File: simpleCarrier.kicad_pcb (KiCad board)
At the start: 4 copper layers, 103 x 99 mm, 132 parts, among them CN1 KH-CL0.5-H2.0-22PIN, CN2 KH-CL0.5-H2.0-22PIN, IC2 RT9187CGB, J1 USB_B, J10 Conn_01x03_Socket, J11 Conn_01x05_Socket, J2 RJ45_RB1-125B8G1A, J3 USB_B, J4 SFW15R-1STE1LF, J5 SFW15R-1STE1LF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

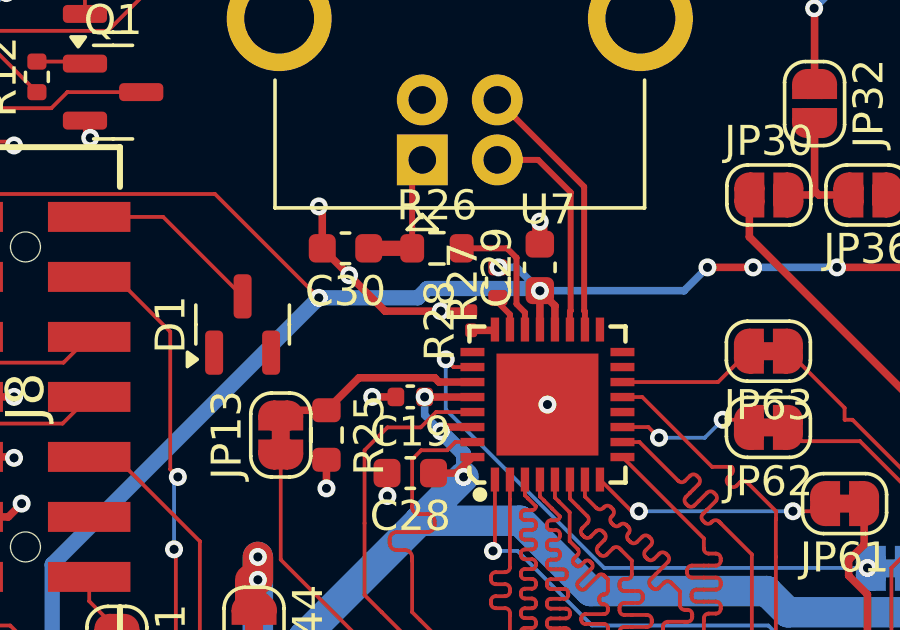
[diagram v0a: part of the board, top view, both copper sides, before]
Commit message: removed all resistors 0201mm, changed to 0402mm
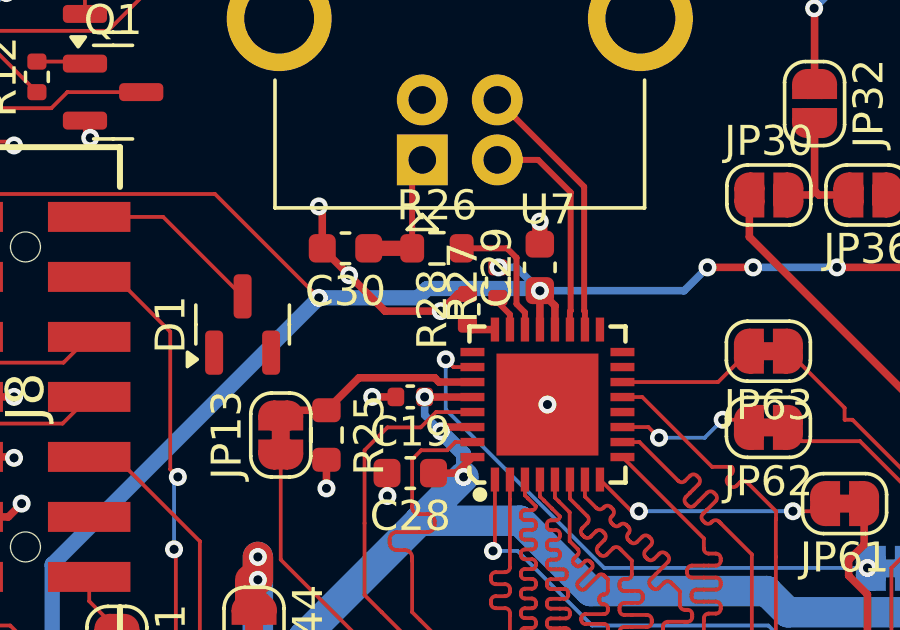
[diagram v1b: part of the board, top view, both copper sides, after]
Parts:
- R28: footprint Resistor_SMD:R_0201_0603Metric -> Resistor_SMD:R_0402_1005Metric
- moved R28 0.40 mm to (116.0, 63.9)

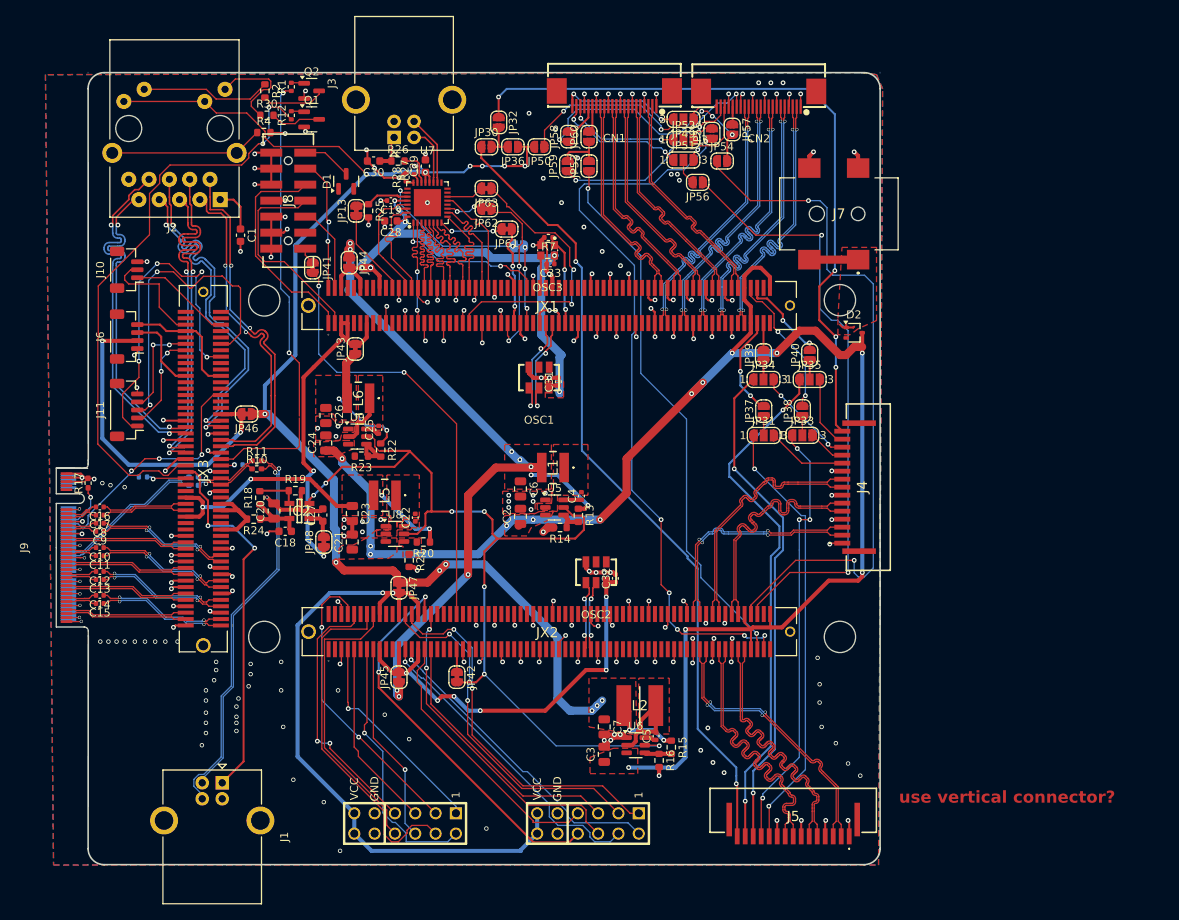
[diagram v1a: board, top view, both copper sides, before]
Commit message: moved to 6 layers, fixing DRC issues
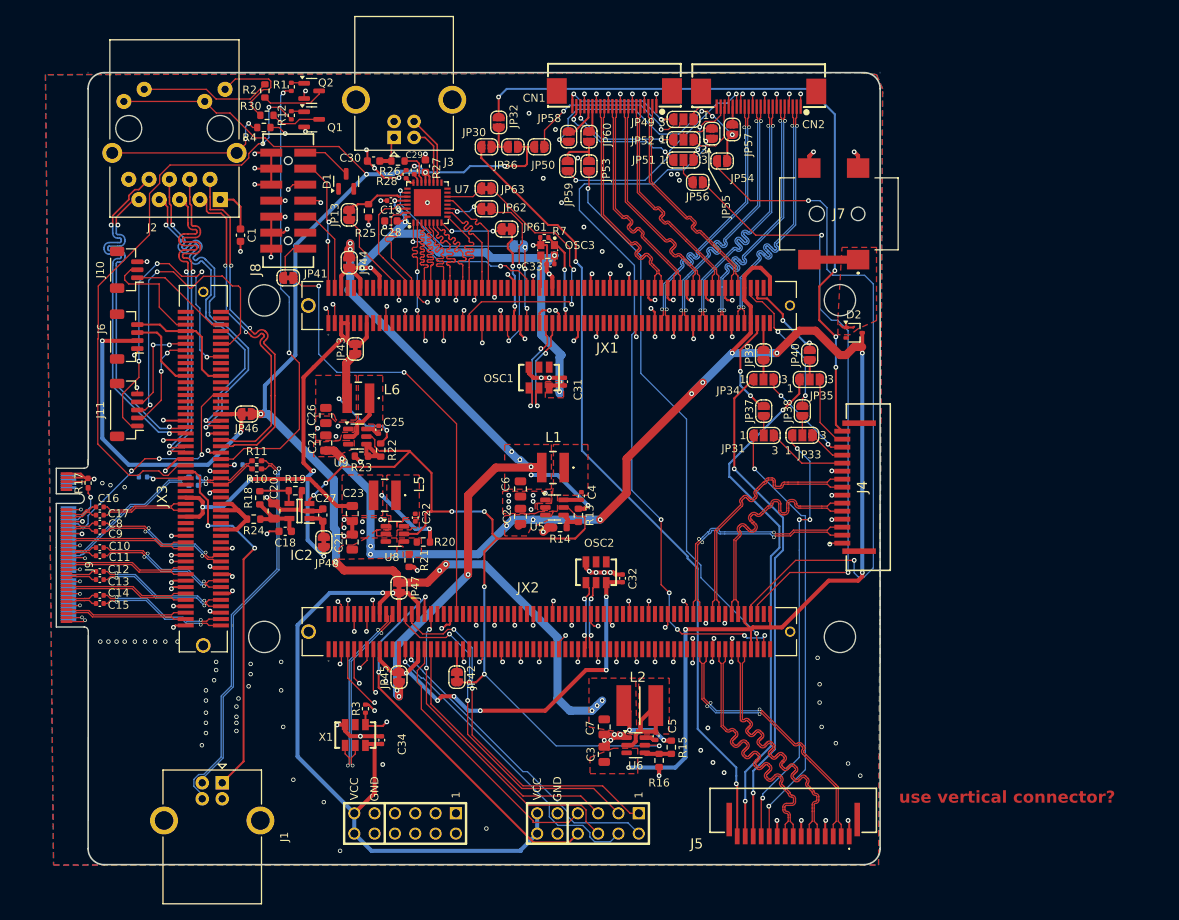
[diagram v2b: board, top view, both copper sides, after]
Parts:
- added C34: 0402,100nF,50V,X7R, Capacitor_SMD:C_0402_1005Metric, F.Cu at (112.9, 134.2)
- added R3: 10k, Resistor_SMD:R_0402_1005Metric, F.Cu at (110.9, 130.3)
- added X1: SIT9121AI-2C1-33E100.000000, my_lib:OSC-SMD_6P-L5.0-W3.2-BL-A, F.Cu at (109.6, 133.6)
- moved JP41 3.30 mm to (101.2, 76.5), turned to 0 degrees
- moved JP13 1.02 mm to (108.8, 68.6)
- moved C32 0.89 mm to (143.0, 114.0)
- moved C31 0.78 mm to (135.8, 89.4)
- moved R4 0.63 mm to (98.2, 57.7)
- moved R7 0.52 mm to (133.2, 71.4)
- moved R28 0.38 mm to (116.0, 63.5)
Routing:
- net JX2_HD_SE_05_GC_P: track 0.00 -> 24.1 mm, vias 0 -> 2
- net JX2_HD_SE_05_GC_N: track 0.00 -> 24.1 mm, vias 0 -> 2
- net JX2_HD_SE_11_N: track 0.00 -> 21.5 mm, vias 0 -> 2
- net JX2_HD_SE_03_P: track 44.1 -> 31.0 mm, vias 0 -> 1
- net VCCO_HD_26: track 82.3 -> 94.2 mm
- net GND: track 310.5 -> 322.4 mm, vias 245 -> 243
- net JX2_HD_SE_02_P: track 33.2 -> 42.1 mm
- net JTAG_TDO: track 25.8 -> 18.8 mm, vias 0 -> 2
- net JTAG_TCK: track 27.6 -> 21.2 mm, vias 0 -> 2
- net JX2_HD_SE_01_N: track 33.1 -> 27.0 mm, vias 2 -> 1
- net JX2_HD_SE_01_P: track 37.2 -> 33.0 mm, vias 2 -> 1
- net /connectors/JTAG_RESET#: track 2.11 -> 5.69 mm
- net JX2_HD_SE_03_N: track 36.3 -> 39.4 mm, vias 0 -> 1
- net Net-(J2-PadSH): track 19.2 -> 21.1 mm, vias 0 -> 2
- net SOM_RESET_IN_N: track 55.1 -> 56.7 mm
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- added copper zone on In3.Cu, net GND
- added copper zone on In4.Cu, net GND
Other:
- board size 103 x 99 mm -> 99 x 99 mm
- copper layers 4 -> 6

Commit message: moved jtag connector, added holes for all power supplies, fixed most of DRC
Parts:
- added J12: Conn_01x01_Pin, Connector_PinHeader_2.00mm:PinHeader_1x01_P2.00mm_Horizontal, B.Cu at (135.1, 93.3)
- added J13: Conn_01x01_Pin, Connector_PinHeader_2.00mm:PinHeader_1x01_P2.00mm_Horizontal, B.Cu at (102.0, 111.6)
- added J14: Conn_01x01_Pin, Connector_PinHeader_2.00mm:PinHeader_1x01_P2.00mm_Horizontal, B.Cu at (128.7, 132.2)
- added J15: Conn_01x01_Pin, Connector_PinHeader_2.00mm:PinHeader_1x01_P2.00mm_Horizontal, B.Cu at (104.5, 115.1)
- added J16: Conn_01x01_Pin, Connector_PinHeader_2.00mm:PinHeader_1x01_P2.00mm_Horizontal, B.Cu at (95.9, 109.9)
- added J17: Conn_01x01_Pin, Connector_PinHeader_2.00mm:PinHeader_1x01_P2.00mm_Horizontal, B.Cu at (99.6, 97.7)
- added J18: Conn_01x01_Pin, Connector_PinHeader_2.00mm:PinHeader_1x01_P2.00mm_Horizontal, B.Cu at (96.7, 90.6)
- added J19: Conn_01x02_Pin, Connector_PinHeader_2.54mm:PinHeader_1x02_P2.54mm_Vertical, B.Cu at (175.6, 71.4)
- added R29: R_0R_0402, Resistor_SMD:R_0402_1005Metric_Pad0.72x0.64mm_HandSolder, B.Cu at (81.8, 103.5)
- added R31: R_0R_0402, Resistor_SMD:R_0402_1005Metric_Pad0.72x0.64mm_HandSolder, F.Cu at (78.7, 103.4)
- added R32: R_0R_0402, Resistor_SMD:R_0402_1005Metric_Pad0.72x0.64mm_HandSolder, B.Cu at (78.6, 100.5)
- R18: value 10.5k -> 680
- moved Q1 16.0 mm to (103.9, 72.6)
- moved Q2 16.0 mm to (103.9, 69.1)
- moved R1 16.0 mm to (101.3, 68.6)
- moved R12 16.0 mm to (101.3, 72.1)
- moved R2 16.0 mm to (98.0, 69.1)
- moved R30 16.0 mm to (98.3, 72.1)
- moved R4 16.0 mm to (97.9, 73.7)
- moved J8 8.65 mm to (101.7, 58.2)
- moved R28 0.52 mm to (115.4, 63.6)
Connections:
- net /PCIE/+3V3 renamed Net-(J9-3.3V-Pad12)
- J9 pad 69: unconnected-(J9-PEDET-Pad69) -> Net-(J9-PEDET)
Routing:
- net Net-(J9-3.3V-Pad12): track 0.00 -> 51.0 mm, vias 0 -> 2
- net ETH_PHY_LED1: track 73.5 -> 34.9 mm
- net ETH_PHY_LED0: track 55.6 -> 36.3 mm
- net JTAG_TMS: track 16.7 -> 33.3 mm
- net JTAG_TDO: track 18.8 -> 33.2 mm
- net Net-(J2-PadL2): track 16.4 -> 26.0 mm
- net JTAG_TDI: track 10.9 -> 20.5 mm, vias 0 -> 2
- net /PCIE/WAKE#: track 0.00 -> 8.94 mm, vias 0 -> 2
- net Net-(J2-PadL4): track 12.5 -> 21.0 mm, vias 0 -> 1
- net Net-(J2-PadSH): track 21.1 -> 29.3 mm, vias 2 -> 0
- net /connectors/JTAG_RESET#: track 5.69 -> 13.6 mm, vias 0 -> 2
- net Net-(D1-K): track 6.21 -> 14.1 mm
- net JTAG_TCK: track 21.2 -> 28.8 mm
- net +3.3V: track 181.2 -> 188.1 mm, vias 13 -> 12
- net Net-(J9-PEDET): track 0.00 -> 5.04 mm, vias 0 -> 2
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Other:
- board size 99 x 99 mm -> 101.7 x 100.9 mm
- board text added: "GND"
- board text added: "MGTRAVTT"
- board text added: "VCCO_HD_26"
- board text added: "VCCO_HP_64"
- board text added: "VCCO_HP_65"
- board text added: "VCCO_HP_66"
- board text added: "VCCO_PSIO_501"
- board text added: "VIN 5-12"
- board text added: "mgtravcc"
- board text removed: "add reset to mio30?"
- board text removed: "use vertical connector?"
